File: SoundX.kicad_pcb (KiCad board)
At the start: 2 copper layers, 60.8 x 99.9 mm, 29 parts, among them CN1 EDGE_CONN, CN2 RAW_AUDIO_OUT, U2 GAL20V8, U3 YM3526, U6 YM3014, U7 LM324, Y1 OSCILLATOR

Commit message: Rough routing complete, even not that rough
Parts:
- added C11: 100n, Capacitor_THT:C_Disc_D7.0mm_W2.5mm_P5.00mm, F.Cu at (179.2, 114.9)
- added CN3: CONN_MIDI_IN, SoundX:DIN5, F.Cu at (171.4, 57.2)
- added CN4: CONN_MIDI_OUT, SoundX:DIN5, F.Cu at (151.6, 57.2)
- added D1: 1n4148, Diode_THT:D_DO-35_SOD27_P2.54mm_Vertical_KathodeUp, F.Cu at (164.0, 78.1)
- added JP3: JMP_POM_GND, Jumper:SolderJumper-2_P1.3mm_Open_RoundedPad1.0x1.5mm, B.Cu at (159.1, 65.4)
- added JP4: JMP_POM_VCC, Jumper:SolderJumper-2_P1.3mm_Open_RoundedPad1.0x1.5mm, B.Cu at (144.1, 65.4)
- added R10: 220, Resistor_THT:R_Axial_DIN0207_L6.3mm_D2.5mm_P2.54mm_Vertical, F.Cu at (179.2, 73.0)
- added R11: 220, Resistor_THT:R_Axial_DIN0207_L6.3mm_D2.5mm_P2.54mm_Vertical, F.Cu at (160.1, 78.1)
- added R12: 220, Resistor_THT:R_Axial_DIN0207_L6.3mm_D2.5mm_P2.54mm_Vertical, F.Cu at (160.1, 73.0)
- added R8: 220, Resistor_THT:R_Axial_DIN0207_L6.3mm_D2.5mm_P2.54mm_Vertical, F.Cu at (164.0, 70.5)
- added R9: 4.7k, Resistor_THT:R_Axial_DIN0207_L6.3mm_D2.5mm_P2.54mm_Vertical, F.Cu at (179.2, 78.1)
- added U2: MOS_6551_ACIA, Package_DIP:DIP-28_W15.24mm_Socket_LongPads, F.Cu at (160.1, 81.9)
- added U4: 6N138, Package_DIP:DIP-8_W7.62mm_Socket_LongPads, F.Cu at (167.8, 70.5)
- added Y2: 3M, Crystal:Crystal_HC49-U_Vertical, F.Cu at (179.7, 95.8)
- R15, R16, R3, R4, R5, R6, R7: footprint Resistor_THT:R_Axial_DIN0207_L6.3mm_D2.5mm_P10.16mm_Horizontal -> Resistor_THT:R_Axial_DIN0207_L6.3mm_D2.5mm_P2.54mm_Vertical
- Y1: value OSCILLATOR -> 3.579545 MHz
- moved FB1 54.6 mm to (136.3, 122.3), turned to 90 degrees
- moved C4 54.5 mm to (126.4, 122.2), turned to 0 degrees
- moved R6 53.9 mm to (126.5, 80.6), turned to 180 degrees
- moved R16 53.3 mm to (124.0, 83.2), turned to 0 degrees
- moved C7 47.0 mm to (126.4, 118.4), turned to 0 degrees
- moved R15 44.6 mm to (131.4, 89.5), turned to 0 degrees
- moved R5 38.3 mm to (134.0, 87.0), turned to 180 degrees
- moved C6 38.0 mm to (136.0, 64.1), turned to 180 degrees
- moved U7 36.9 mm to (129.7, 67.9), turned to 0 degrees
- moved R4 31.1 mm to (141.1, 75.6), turned to 270 degrees
- moved C10 31.0 mm to (144.9, 70.5), turned to 270 degrees
- moved Y1 29.6 mm to (134.0, 113.3), turned to 90 degrees
- moved R3 29.0 mm to (141.1, 70.5)
- moved C3 28.4 mm to (141.1, 83.2), turned to 0 degrees
- moved C9 27.3 mm to (125.9, 75.6), turned to 90 degrees
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- renumbered U2 to U1
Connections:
- R5 pad 1: Net-(R5-Pad1) -> Net-(R15-Pad2)
- R5 pad 2: Net-(R15-Pad2) -> Net-(R5-Pad2)
- R6 pad 1: Net-(R5-Pad1) -> Net-(C1-Pad1)
- R6 pad 2: Net-(C1-Pad1) -> Net-(R5-Pad2)
- U1 pad 15: /~kbd_cs -> /~midi_cs
- U1 pad 19: /~ym_cs -> /a9
- U1 pad 20: /~ym_rd -> /~ym_cs
- U1 pad 21: /a9 -> /~ym_rd
- U7 pad 6: Net-(R5-Pad1) -> Net-(R5-Pad2)
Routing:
- net /ext_audio: track 24.2 -> 130.3 mm, vias 1 -> 3
- net +5V: track 124.7 -> 225.8 mm, vias 0 -> 3
- net /d0: track 37.4 -> 98.9 mm, vias 0 -> 2
- net /~irq: track 42.7 -> 97.0 mm, vias 0 -> 1
- net /rxd_ttl: track 0.00 -> 53.9 mm, vias 0 -> 1
- net /d1: track 43.0 -> 94.8 mm, vias 0 -> 2
- net /r_~w: track 46.5 -> 96.2 mm, vias 2 -> 3
- net /~midi_cs: track 0.00 -> 47.8 mm, vias 0 -> 3
- net /phi2: track 23.1 -> 65.0 mm
- net Net-(R5-Pad1): track 40.1 -> 0.00 mm
- net /~reset: track 45.5 -> 79.0 mm
- net /a0: track 14.7 -> 45.7 mm, vias 0 -> 1
- net /d7: track 57.9 -> 88.4 mm, vias 0 -> 1
- net /txd_ttl: track 0.00 -> 28.1 mm
- net /d6: track 57.0 -> 84.9 mm, vias 0 -> 1
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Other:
- board text added: "6551 (ACIA) OR COMPATIBLE"
- board text added: "IN"
- board text added: "OUT"
- board text added: "OUTPUT"
- board text removed: "RAW"

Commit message: First round of improvements by @kinmami
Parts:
- added C12: 22p, Capacitor_THT:C_Disc_D7.0mm_W2.5mm_P5.00mm, F.Cu at (179.2, 87.0)
- added C13: 220p, Capacitor_THT:C_Disc_D7.0mm_W2.5mm_P5.00mm, F.Cu at (136.0, 87.0)
- added C14: 100n, Capacitor_THT:C_Disc_D7.0mm_W2.5mm_P5.00mm, F.Cu at (131.4, 135.8)
- added C15: 10u, Capacitor_THT:CP_Radial_D5.0mm_P2.00mm, F.Cu at (150.1, 81.6)
- added FB1: FERRITE, Inductor_THT:L_Radial_D6.0mm_P4.00mm, F.Cu at (127.3, 130.8)
- added R1: 1M, Resistor_THT:R_Axial_DIN0207_L6.3mm_D2.5mm_P2.54mm_Vertical, F.Cu at (179.2, 103.5)
- C1: value 4.7u -> 10u
- R16: value 4.7k -> 10k
- moved R15 5.60 mm to (136.1, 92.6), turned to 90 degrees
- moved C4 3.81 mm to (126.4, 118.4)
- moved C7 3.81 mm to (126.4, 122.2)
- moved R5 3.06 mm to (133.7, 90.0), turned to 270 degrees
- moved R7 2.90 mm to (131.2, 92.6), turned to 90 degrees
- moved R16 2.54 mm to (124.0, 80.6), turned to 270 degrees
- moved R6 2.54 mm to (126.5, 83.2), turned to 90 degrees
- moved Y2 2.54 mm to (179.7, 98.3)
- moved C5 0.38 mm to (154.7, 82.5)
- renumbered FB1 to FB2, FB2 to FB3
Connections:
- net Net-(U2-Pad6) renamed /q+
- net Net-(U2-Pad7) renamed /q-
- CN1 pad 2: +5V -> Net-(C14-Pad1)
- CN1 pad 3: +5V -> Net-(C14-Pad1)
- FB3 pad 1: Net-(FB2-Pad1) -> /clock
- FB3 pad 2: Net-(FB2-Pad2) -> Net-(FB3-Pad2)
- R7 pad 1: /clock -> Net-(FB3-Pad2)
- R7 pad 2: Net-(FB2-Pad1) -> Net-(R7-Pad2)
- Y1 pad 8: Net-(FB2-Pad2) -> Net-(R7-Pad2)
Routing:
- net Net-(C14-Pad1): track 0.00 -> 24.0 mm
- net /q+: track 21.2 -> 40.5 mm
- net Net-(C13-Pad1): track 13.6 -> 32.6 mm
- net Net-(R7-Pad2): track 0.00 -> 17.6 mm
- net Net-(FB2-Pad2): track 12.3 -> 0.00 mm
- net +5V: track 225.8 -> 213.7 mm
- net /~ym_cs: track 41.7 -> 30.9 mm
- net /~ym_rd: track 39.9 -> 31.2 mm
- net /d1: track 94.8 -> 103.1 mm, vias 2 -> 4
- net /d0: track 98.9 -> 107.1 mm, vias 2 -> 4
- net Net-(FB2-Pad1): track 6.74 -> 0.00 mm
- net /clock: track 25.0 -> 30.9 mm
- net /q-: track 20.1 -> 25.4 mm
- net Net-(FB3-Pad2): track 0.00 -> 5.14 mm
- net Net-(R15-Pad2): track 43.1 -> 46.9 mm
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- added copper zone on F.Cu, net Net-(C14-Pad1)

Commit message: Add logo
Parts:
- added V1: LOGO, SoundX:logo, F.Cu at (144.3, 136.0)
- moved V0 43.7 mm to (174.0, 135.8)

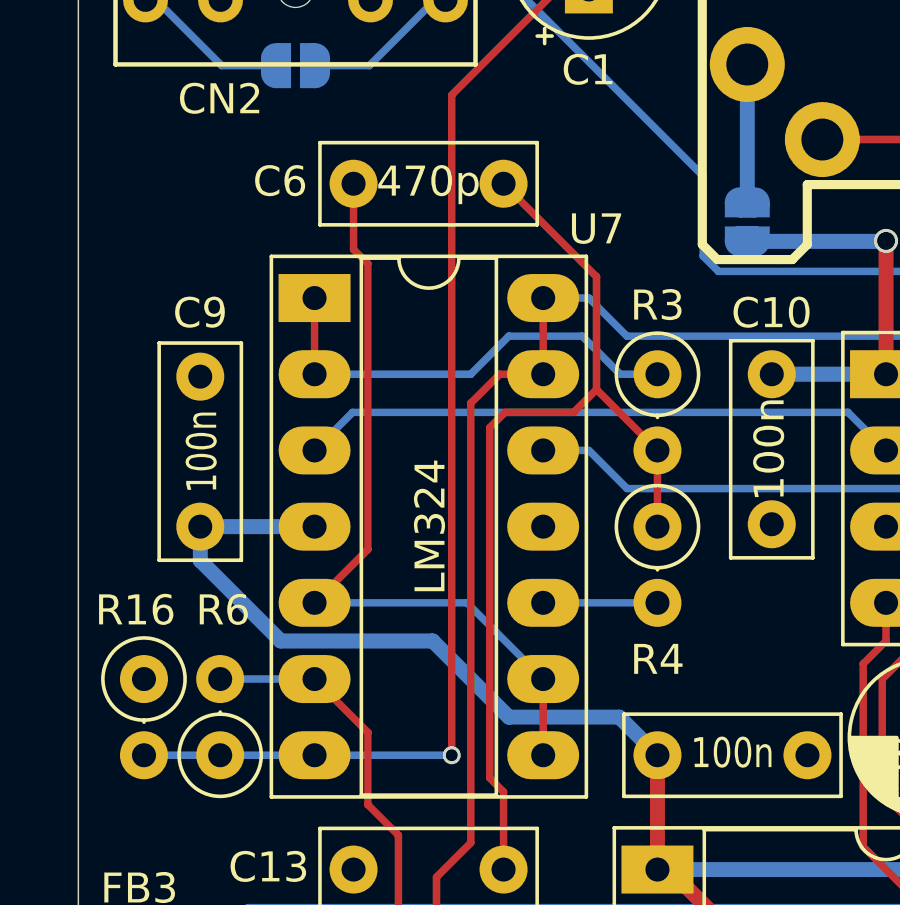
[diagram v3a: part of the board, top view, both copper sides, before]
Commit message: Add filter bypass jumper
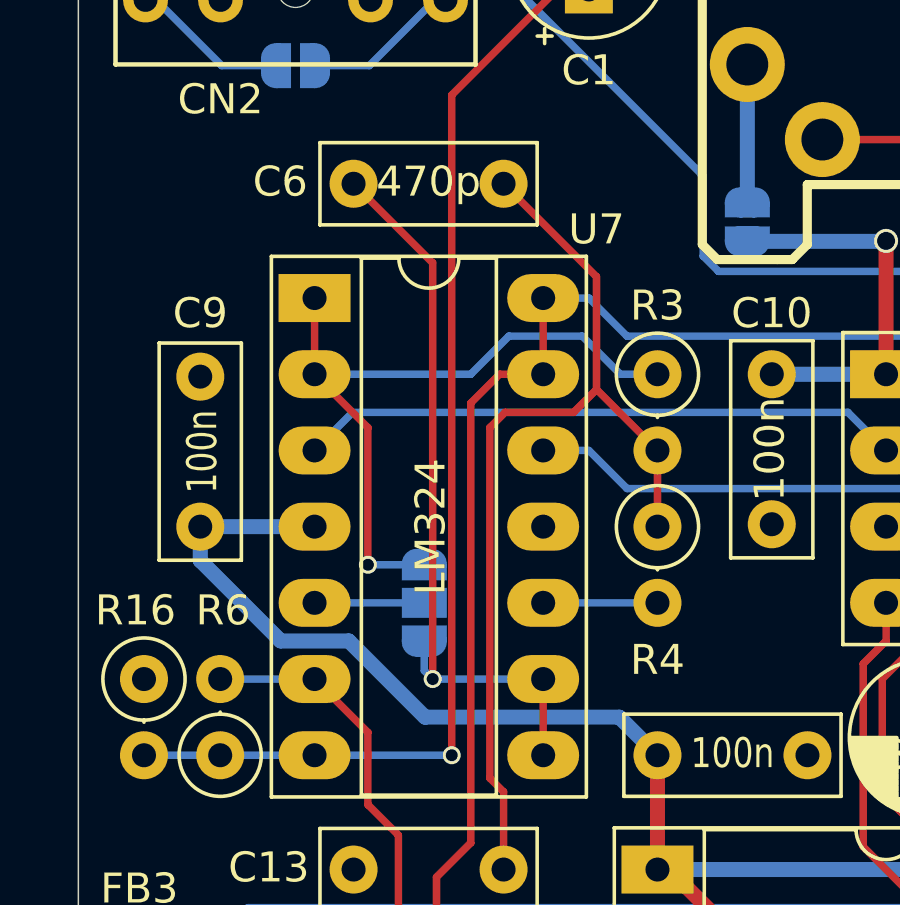
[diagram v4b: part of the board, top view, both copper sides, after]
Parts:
- added JP5: JMP_FILTER_BYPASS, Jumper:SolderJumper-3_P1.3mm_Open_RoundedPad1.0x1.5mm, B.Cu at (133.3, 78.1)
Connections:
- U7 pad 5: Net-(C6-Pad2) -> /amp_in
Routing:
- net Net-(JP5-Pad3): track 15.0 -> 24.0 mm, vias 0 -> 1
- net /amp_in: track 0.00 -> 3.66 mm
- net Net-(C6-Pad2): track 26.1 -> 25.2 mm, vias 0 -> 1
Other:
- board text added: "BYP"
- board text added: "ON"

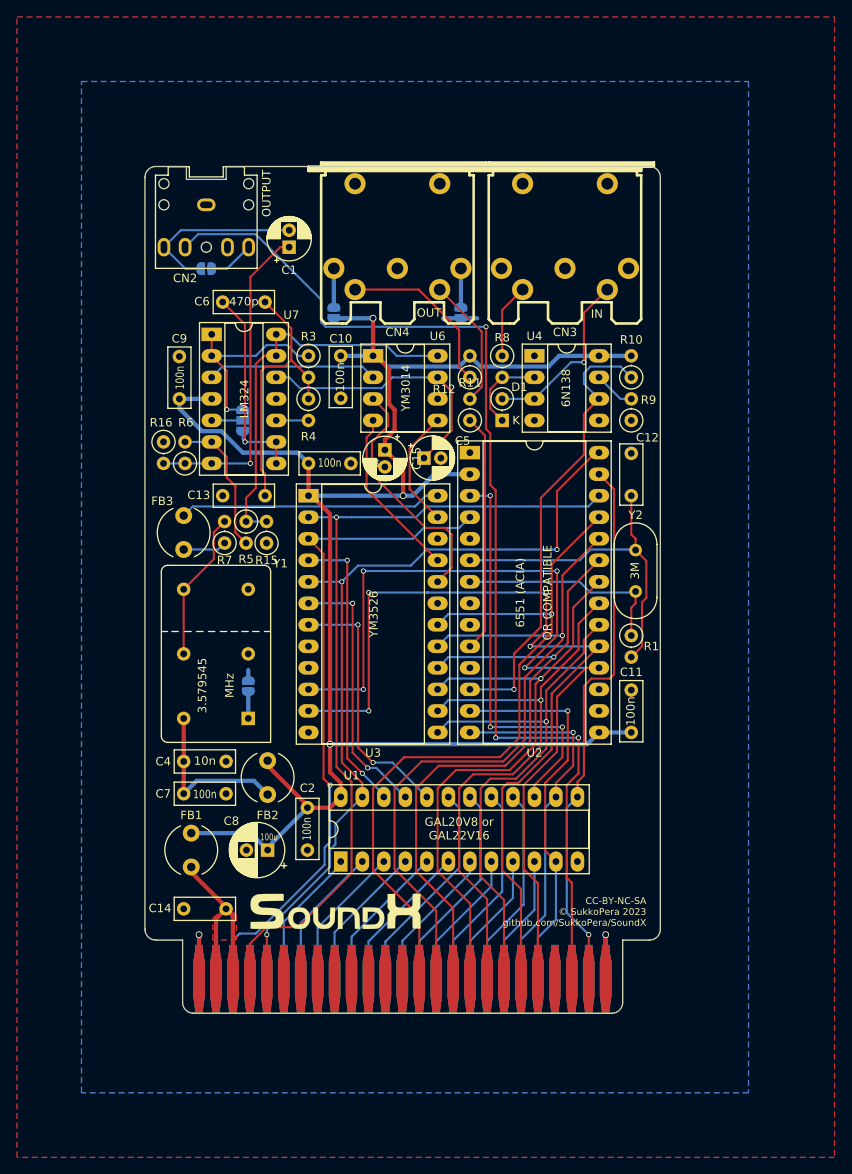
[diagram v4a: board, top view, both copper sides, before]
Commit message: Tidy up silkscreen
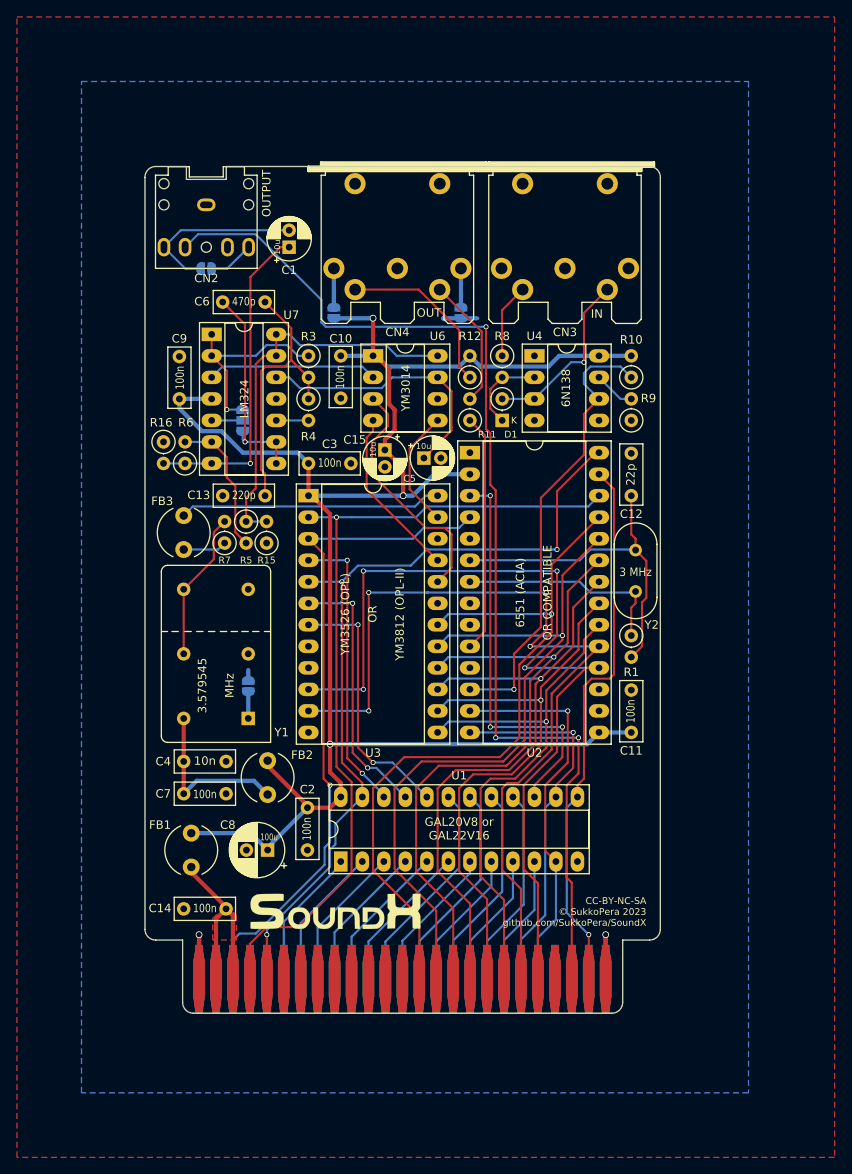
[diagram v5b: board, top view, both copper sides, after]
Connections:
- net Net-(C6-Pad2) renamed /flt_out
- net Net-(JP5-Pad3) renamed /flt_in
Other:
- board text added: "3 MHz"
- board text added: "YM3526 (OPL) OR YM3812 (OPL-II)"

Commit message: Final touches
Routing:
- net /ext_audio: track 130.3 -> 134.2 mm
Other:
- board text added: "CC-BY-NC-SA © SukkoPera/Kinmami 2023 github.com/SukkoPera/SoundX"
- board text removed: "CC-BY-NC-SA © SukkoPera 2023 github.com/SukkoPera/SoundX"

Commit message: Second round of improvements by @kinmami
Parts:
- moved C1 14.3 mm to (126.0, 64.1), turned to 180 degrees
- moved FB1 2.19 mm to (126.4, 128.8), turned to 0 degrees
- moved C15 1.97 mm to (150.1, 83.6), turned to 90 degrees
- moved C8 1.30 mm to (135.7, 127.6), turned to 270 degrees
- moved C2 0.13 mm to (141.1, 123.8)
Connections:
- R7 pad 1: Net-(FB3-Pad2) -> Net-(R7-Pad1)
- R7 pad 2: Net-(R7-Pad2) -> Net-(FB3-Pad2)
- Y1 pad 8: Net-(R7-Pad2) -> Net-(R7-Pad1)
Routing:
- net Net-(R7-Pad2): track 17.6 -> 0.00 mm
- net Net-(R7-Pad1): track 0.00 -> 15.1 mm
- net Net-(C1-Pad2): track 21.0 -> 11.9 mm
- net +5V: track 213.7 -> 219.5 mm, vias 3 -> 4
- net /rxd_ttl: track 53.9 -> 48.5 mm
- net /dac_clk: track 29.0 -> 26.3 mm
- net Net-(C14-Pad1): track 24.0 -> 26.3 mm
- net Net-(C1-Pad1): track 38.3 -> 36.1 mm, vias 1 -> 2
- net Net-(FB3-Pad2): track 5.14 -> 6.19 mm
- net Net-(CN3-Pad5): track 21.2 -> 20.3 mm, vias 1 -> 0
- net /~irq: track 97.7 -> 98.4 mm
- net /~ym_rd: track 31.2 -> 32.0 mm
- net /~ym_cs: track 30.9 -> 31.6 mm
- net /ym_a0: track 34.3 -> 35.0 mm
- net /r_~w: track 97.2 -> 96.6 mm
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
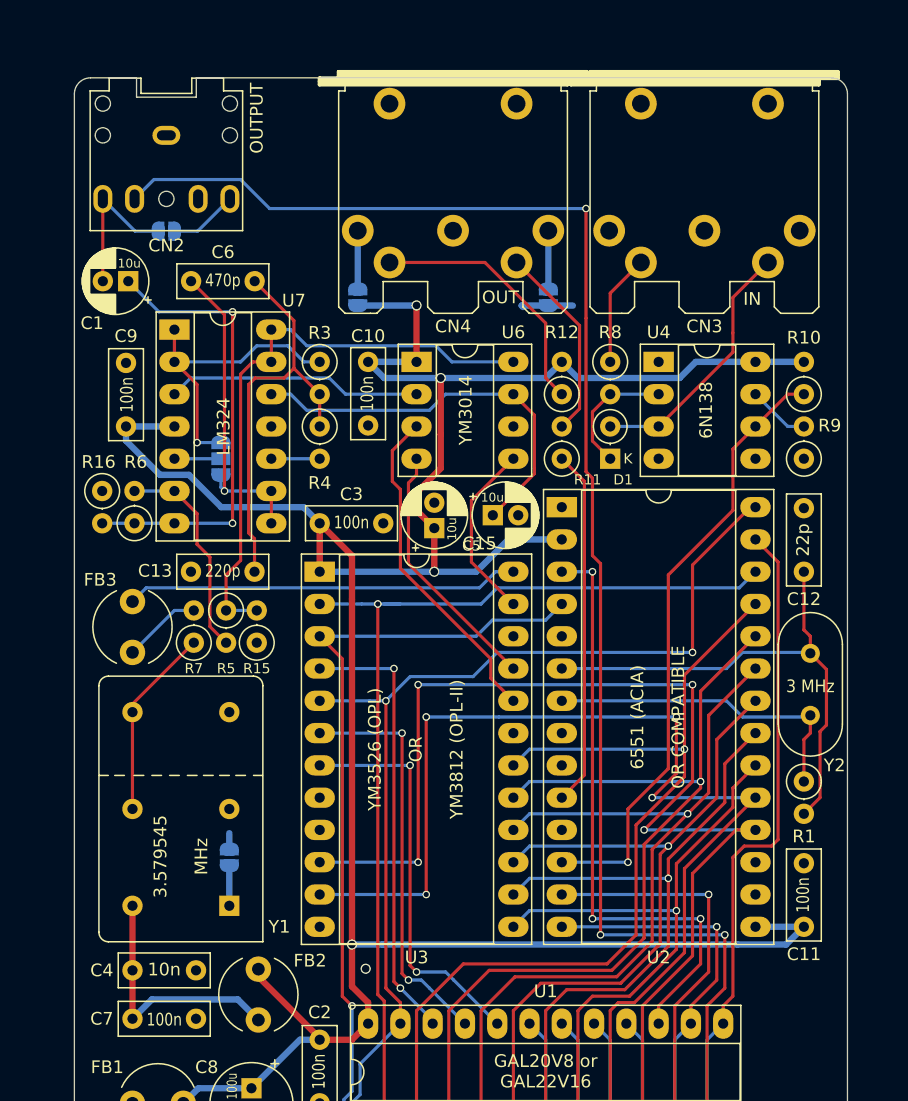
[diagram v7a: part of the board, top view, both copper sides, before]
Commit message: Add output gain pot
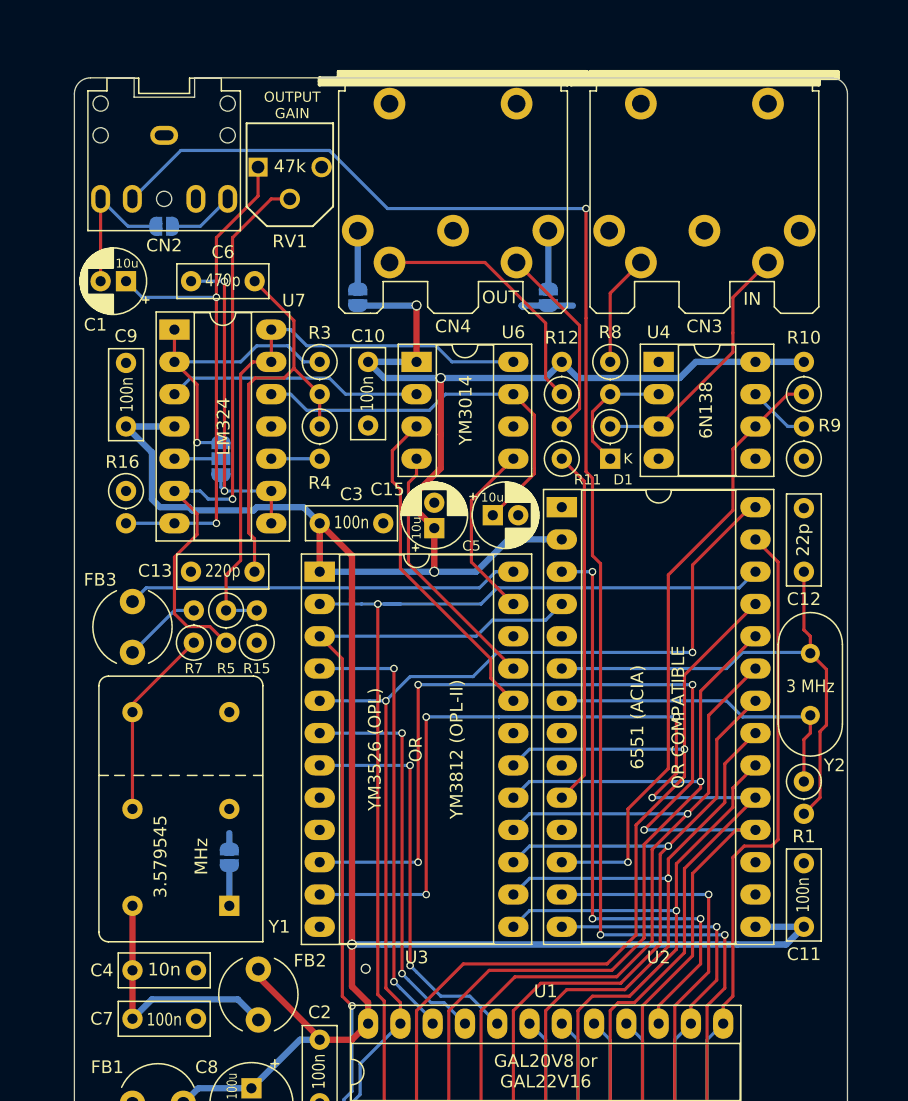
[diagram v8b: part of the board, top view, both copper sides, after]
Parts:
- removed R6: 27k, Resistor_THT:R_Axial_DIN0207_L6.3mm_D2.5mm_P2.54mm_Vertical
- added RV1: 47k, SoundX:Pot_Bourns_3306P, F.Cu at (138.7, 56.4)
- moved R16 1.88 mm to (125.9, 80.6)
- moved JP2 0.42 mm to (128.9, 59.8)
- moved CN2 0.18 mm to (128.9, 52.7)
- moved C1 0.17 mm to (125.9, 64.1)
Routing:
- net Net-(R5-Pad2): track 16.8 -> 47.3 mm, vias 0 -> 1
- net Net-(C1-Pad1): track 36.1 -> 43.5 mm
- net /ext_audio: track 133.8 -> 135.8 mm
- net +5V: track 219.5 -> 221.2 mm
- net /flt_out: track 25.2 -> 26.7 mm, vias 1 -> 2
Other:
- outline, holes or cut-outs redrawn
- board text added: "OUTPUT GAIN"
- board text removed: "OUTPUT"
